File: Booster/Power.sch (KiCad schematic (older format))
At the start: 7 parts, among them J301 15VDC, U301 LM7805_TO220

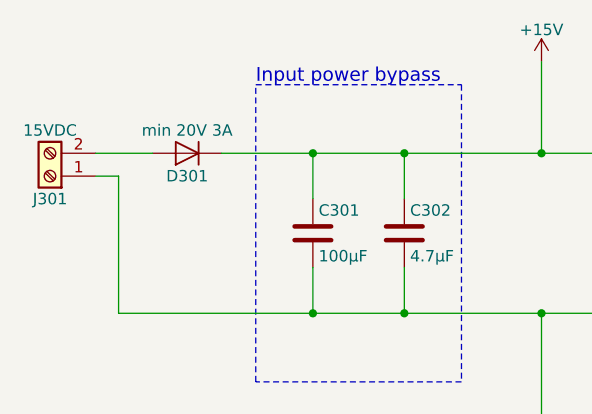
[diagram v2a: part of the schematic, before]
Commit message: Assigned footprints & minor adjustments.
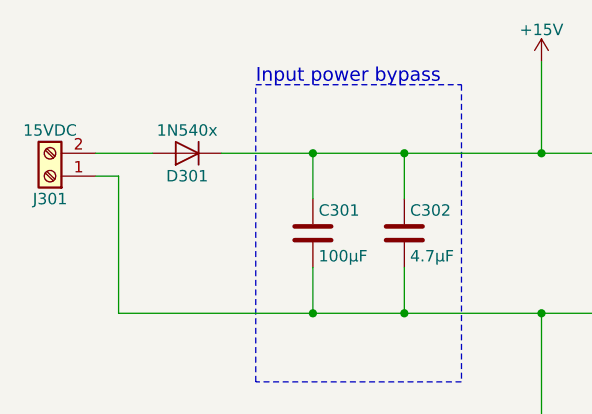
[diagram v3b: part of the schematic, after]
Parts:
- C301, C303, C304: footprint (none) -> Capacitors_SMD:C_0805
- C302: footprint (none) -> Capacitors_THT:CP_Radial_D5.0mm_P2.00mm
- D301: value min 20V 3A -> 1N540x; footprint (none) -> Diodes_THT:D_DO-201AD_P5.08mm_Vertical_AnodeUp
- J301: footprint (none) -> Connectors_Terminal_Blocks:TerminalBlock_bornier-2_P5.08mm
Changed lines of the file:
@@
 F 0 "C303" H 6675 3900 50  0000 L CNN
 F 1 "330nF" H 6675 3700 50  0000 L CNN
-F 2 "" H 6688 3650 50  0001 C CNN
+F 2 "Capacitors_SMD:C_0805" H 6688 3650 50  0001 C CNN
 F 3 "" H 6650 3800 50  0001 C CNN
 	1    6650 3800
@@
 F 0 "C304" H 7625 3900 50  0000 L CNN
 F 1 "100nF" H 7625 3700 50  0000 L CNN
-F 2 "" H 7638 3650 50  0001 C CNN
+F 2 "Capacitors_SMD:C_0805" H 7638 3650 50  0001 C CNN
 F 3 "" H 7600 3800 50  0001 C CNN
 	1    7600 3800
@@
 F 0 "J301" H 3200 3600 50  0000 C CNN
 F 1 "15VDC" H 3200 3300 50  0000 C CNN
-F 2 "" H 3200 3500 50  0001 C CNN
+F 2 "Connectors_Terminal_Blocks:TerminalBlock_bornier-2_P5.08mm" H 3200 3500 50  0001 C CNN
 F 3 "" H 3200 3500 50  0001 C CNN
 	1    3200 3500
@@
 F 0 "C301" H 4375 3850 50  0000 L CNN
 F 1 "100µF" H 4375 3650 50  0000 L CNN
-F 2 "" H 4388 3600 50  0001 C CNN
+F 2 "Capacitors_SMD:C_0805" H 4388 3600 50  0001 C CNN
 F 3 "" H 4350 3750 50  0001 C CNN
 	1    4350 3750
@@
 F 0 "C302" H 4775 3850 50  0000 L CNN
 F 1 "4.7µF" H 4775 3650 50  0000 L CNN
-F 2 "" H 4788 3600 50  0001 C CNN
+F 2 "Capacitors_THT:CP_Radial_D5.0mm_P2.00mm" H 4788 3600 50  0001 C CNN
 F 3 "" H 4750 3750 50  0001 C CNN
 	1    4750 3750
@@
 P 3800 3400
 F 0 "D301" H 3800 3500 50  0000 C CNN
-F 1 "min 20V 3A" H 3800 3300 50  0000 C CNN
-F 2 "" H 3800 3400 50  0001 C CNN
+F 1 "1N540x" H 3800 3300 50  0000 C CNN
+F 2 "Diodes_THT:D_DO-201AD_P5.08mm_Vertical_AnodeUp" H 3800 3400 50  0001 C CNN
 F 3 "" H 3800 3400 50  0001 C CNN
 	1    3800 3400

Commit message: Started working on the PCB layout. Just getting a rough idea for now.
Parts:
- C301: footprint Capacitors_SMD:C_0805 -> Capacitors_THT:CP_Radial_D6.3mm_P2.50mm
- U301: footprint TO_SOT_Packages_THT:TO-220_Vertical -> TO_SOT_Packages_THT:TO-220-3_Vertical
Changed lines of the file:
@@
 F 0 "U301" H 7000 3525 50  0000 C CNN
 F 1 "LM7805_TO220" H 7150 3525 50  0000 L CNN
-F 2 "TO_SOT_Packages_THT:TO-220_Vertical" H 7150 3625 50  0001 C CIN
+F 2 "TO_SOT_Packages_THT:TO-220-3_Vertical" H 7150 3625 50  0001 C CIN
 F 3 "" H 7150 3350 50  0001 C CNN
 	1    7150 3400
@@
 F 0 "C301" H 4375 3850 50  0000 L CNN
 F 1 "100µF" H 4375 3650 50  0000 L CNN
-F 2 "Capacitors_SMD:C_0805" H 4388 3600 50  0001 C CNN
+F 2 "Capacitors_THT:CP_Radial_D6.3mm_P2.50mm" H 4388 3600 50  0001 C CNN
 F 3 "" H 4350 3750 50  0001 C CNN
 	1    4350 3750

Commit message: Starting to add traces. Minor schematic changes to aid routing.
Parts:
- U301: footprint TO_SOT_Packages_THT:TO-220-3_Vertical -> TO_SOT_Packages_SMD:SOT-89-3
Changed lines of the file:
@@
 F 0 "U301" H 7000 3525 50  0000 C CNN
 F 1 "LM7805_TO220" H 7150 3525 50  0000 L CNN
-F 2 "TO_SOT_Packages_THT:TO-220-3_Vertical" H 7150 3625 50  0001 C CIN
+F 2 "TO_SOT_Packages_SMD:SOT-89-3" H 7150 3625 50  0001 C CIN
 F 3 "" H 7150 3350 50  0001 C CNN
 	1    7150 3400
@@
 $EndComp
 $Comp
-L GND #PWR011
+L GND #PWR302
 U 1 1 59E90316
 P 5350 4550
-F 0 "#PWR011" H 5350 4300 50  0001 C CNN
+F 0 "#PWR302" H 5350 4300 50  0001 C CNN
 F 1 "GND" H 5350 4400 50  0000 C CNN
 F 2 "" H 5350 4550 50  0001 C CNN
@@
 	7450 3400 8250 3400
 $Comp
-L +5V #PWR012
+L +5V #PWR303
 U 1 1 59E9089F
 P 8250 3050
-F 0 "#PWR012" H 8250 2900 50  0001 C CNN
+F 0 "#PWR303" H 8250 2900 50  0001 C CNN
 F 1 "+5V" H 8250 3190 50  0000 C CNN
 F 2 "" H 8250 3050 50  0001 C CNN
@@
 	3500 3500 3500 4100
 $Comp
-L +15V #PWR013
+L +15V #PWR301
 U 1 1 5A093AB5
 P 5350 3000
-F 0 "#PWR013" H 5350 2850 50  0001 C CNN
+F 0 "#PWR301" H 5350 2850 50  0001 C CNN
 F 1 "+15V" H 5350 3140 50  0000 C CNN
 F 2 "" H 5350 3000 50  0000 C CNN

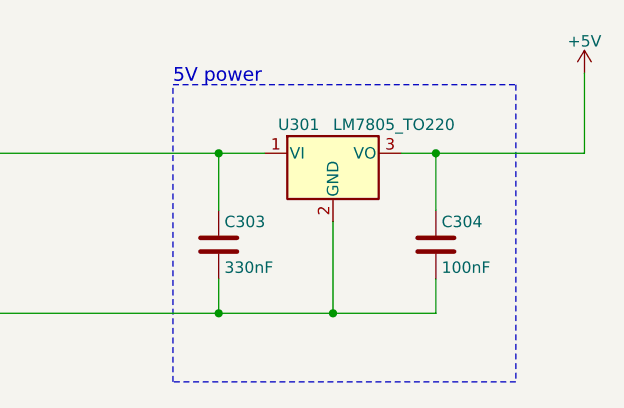
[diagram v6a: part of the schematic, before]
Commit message: Increased resistor sizes on opt couplers and LED's to ensure the 78L05 can deliver enough power.
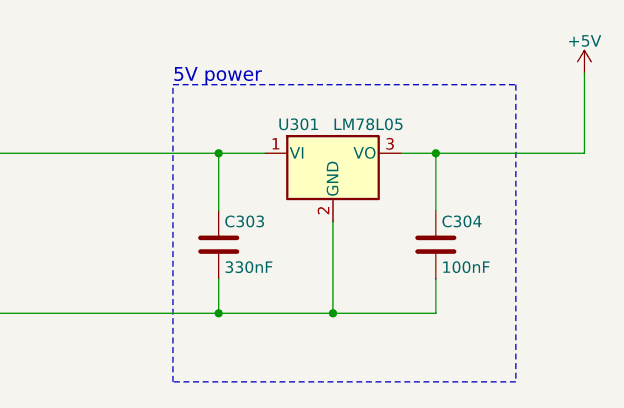
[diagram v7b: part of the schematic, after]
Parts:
- U301: value LM7805_TO220 -> LM78L05
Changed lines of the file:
@@
 P 7150 3400
 F 0 "U301" H 7000 3525 50  0000 C CNN
-F 1 "LM7805_TO220" H 7150 3525 50  0000 L CNN
+F 1 "LM78L05" H 7150 3525 50  0000 L CNN
 F 2 "TO_SOT_Packages_SMD:SOT-89-3" H 7150 3625 50  0001 C CIN
 F 3 "" H 7150 3350 50  0001 C CNN

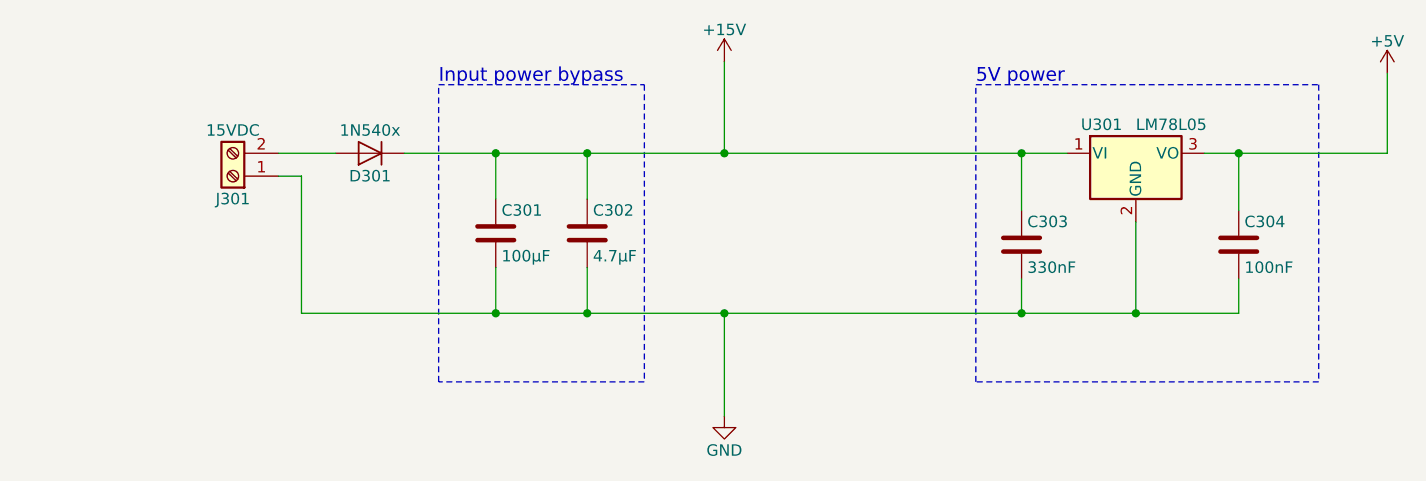
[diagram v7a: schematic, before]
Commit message: Changed booster reversed polarity protection from a diode to a p channel mosfet to reduce the voltage drop.
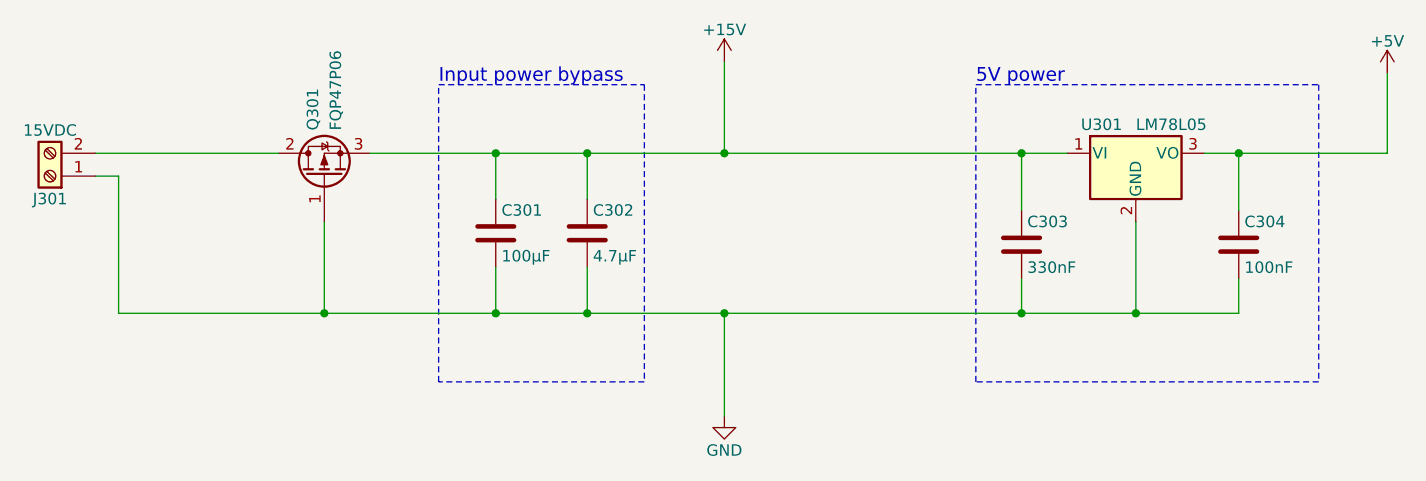
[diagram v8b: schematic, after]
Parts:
- removed D301: 1N540x, Diodes_THT:D_DO-201AD_P5.08mm_Vertical_AnodeUp, symbol D
- added Q301: FQP47P06, TO_SOT_Packages_THT:TO-220-3_Vertical, symbol Q_PMOS_GDS
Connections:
- net +15V: now also Q301.3 (S)
- net GND: now also Q301.1 (G)
- net at J301.2 (Pin_2): now also Q301.2 (D)
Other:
- moved on the sheet: J301
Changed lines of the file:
@@
 L Screw_Terminal_01x02 J301
 U 1 1 59E9033D
-P 3200 3500
-F 0 "J301" H 3200 3600 50  0000 C CNN
-F 1 "15VDC" H 3200 3300 50  0000 C CNN
-F 2 "Connectors_Terminal_Blocks:TerminalBlock_bornier-2_P5.08mm" H 3200 3500 50  0001 C CNN
-F 3 "" H 3200 3500 50  0001 C CNN
-	1    3200 3500
+P 2400 3500
+F 0 "J301" H 2400 3600 50  0000 C CNN
+F 1 "15VDC" H 2400 3300 50  0000 C CNN
+F 2 "Connectors_Terminal_Blocks:TerminalBlock_bornier-2_P5.08mm" H 2400 3500 50  0001 C CNN
+F 3 "" H 2400 3500 50  0001 C CNN
+	1    2400 3500
 	-1   0    0    1
 $EndComp
@@
 Connection ~ 6650 4100
 Wire Wire Line
-	3400 3500 3500 3500
+	2600 3500 2700 3500
 Wire Wire Line
 	7600 4100 7600 3950
@@
 Connection ~ 7150 4100
 Wire Wire Line
-	3500 4100 7600 4100
+	2700 4100 7600 4100
 Wire Wire Line
 	6650 4100 6650 3950
 Connection ~ 6650 3400
-Wire Wire Line
-	3950 3400 6850 3400
 Wire Wire Line
 	7450 3400 8250 3400
@@
 5V power
 Wire Wire Line
-	5350 3000 5350 3400
+	5350 3400 5350 3000
 Connection ~ 5350 3400
 Wire Wire Line
@@
 Connection ~ 5350 4100
 Wire Wire Line
-	3500 3500 3500 4100
+	2700 3500 2700 4100
 $Comp
 L +15V #PWR013
@@
 Wire Wire Line
 	8250 3400 8250 3050
+Wire Wire Line
+	2600 3400 3400 3400
+Wire Wire Line
+	3800 3400 6850 3400
 $Comp
-L D D301
-U 1 1 5A0E87C4
-P 3800 3400
-F 0 "D301" H 3800 3500 50  0000 C CNN
-F 1 "1N540x" H 3800 3300 50  0000 C CNN
-F 2 "Diodes_THT:D_DO-201AD_P5.08mm_Vertical_AnodeUp" H 3800 3400 50  0001 C CNN
-F 3 "" H 3800 3400 50  0001 C CNN
-	1    3800 3400
-	-1   0    0    1
+L Q_PMOS_GDS Q301
+U 1 1 5A624B3C
+P 3600 3500
+F 0 "Q301" H 3800 3550 50  0000 L CNN
+F 1 "FQP47P06" H 3800 3450 50  0000 L CNN
+F 2 "TO_SOT_Packages_THT:TO-220-3_Vertical" H 3800 3600 50  0001 C CNN
+F 3 "" H 3600 3500 50  0001 C CNN
+	1    3600 3500
+	0    -1   -1   0
 $EndComp
 Wire Wire Line
-	3400 3400 3650 3400
+	3600 3700 3600 4100
+Connection ~ 3600 4100
 $EndSCHEMATC
